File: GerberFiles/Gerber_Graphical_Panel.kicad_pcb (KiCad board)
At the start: 2 copper layers, 60.6 x 128.5 mm, 0 parts

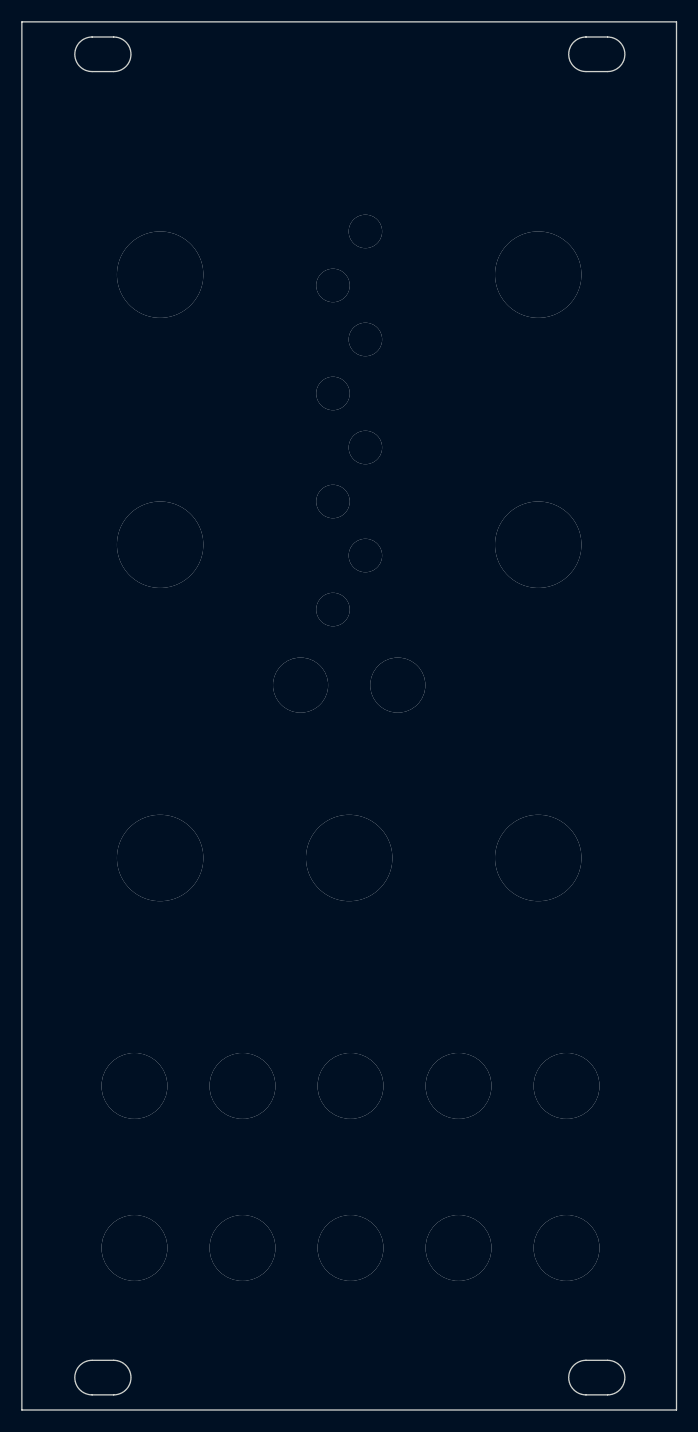
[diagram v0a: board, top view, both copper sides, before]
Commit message: Added copper plane to front/back
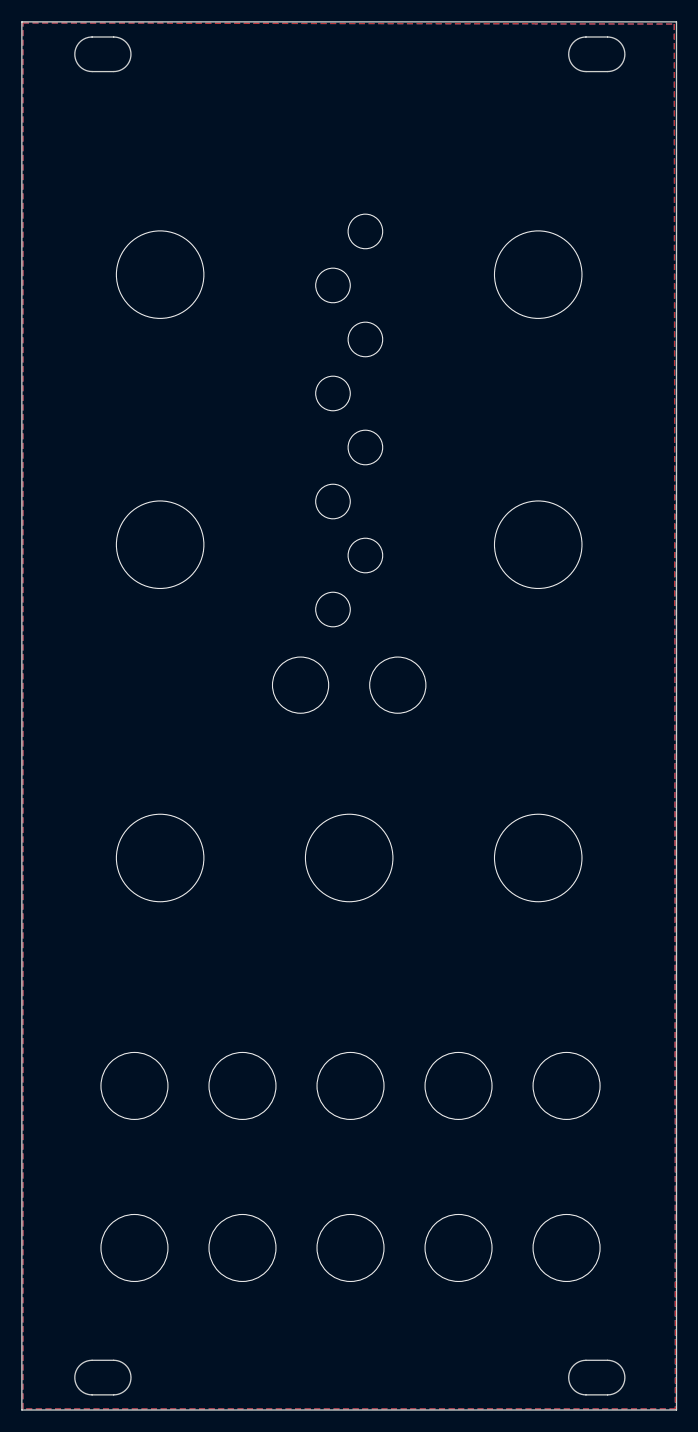
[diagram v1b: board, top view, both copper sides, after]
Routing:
- added copper zone on B.Cu, net (none)
- added copper zone on F.Cu, net (none)
